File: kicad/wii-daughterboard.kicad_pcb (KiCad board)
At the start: 2 copper layers, 35.2 x 47.6 mm, 34 parts, among them J1 Data, J10 USB, J11 A/V Out, J12 Bluetooth Sync, J14 Case Panel, J2 DC In, J3 GameCube 1, J4 GameCube 2, J5 Bluetooth, J6 GameCube 3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

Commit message: v2.0
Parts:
- removed J14: Case Panel, project-footprints:SFV4R3STBE1HLF
- removed U4: MIC94053YC6-TR, Package_TO_SOT_SMD:SOT-363_SC-70-6_Handsoldering
- added J9: Fr. Panel, project-footprints:SFV4R3STBE1HLF, F.Cu at (77.8, 76.4)
- added Q1: DMG2301L, Package_TO_SOT_SMD:SOT-23_Handsoldering, F.Cu at (74.1, 59.0)
- added R8: 100R, Resistor_SMD:R_0603_1608Metric_Pad1.05x0.95mm_HandSolder, F.Cu at (72.0, 74.4)
- added TP1: 5V, TestPoint:TestPoint_Pad_D1.0mm, F.Cu at (75.5, 56.0)
- added TP2: 3V3, TestPoint:TestPoint_Pad_D1.0mm, F.Cu at (87.4, 55.9)
- added TP3: 1V15, TestPoint:TestPoint_Pad_D1.0mm, F.Cu at (99.3, 55.9)
- added TP4: 1V0, TestPoint:TestPoint_Pad_D1.0mm, F.Cu at (111.2, 55.9)
- C1, C2, C3, C4, C5, C6, L1, L2, L3, U1, U2, U3: moved to F.Cu
- J10: value USB -> A/V Pwr; footprint Connector_JST:JST_SH_BM04B-SRSS-TB_1x04-1MP_P1.00mm_Vertical -> Connector_JST:JST_PH_B2B-PH-SM4-TB_1x02-1MP_P2.00mm_Vertical
- J11: value A/V Out -> Sync; footprint Connector_JST:JST_PH_B2B-PH-SM4-TB_1x02-1MP_P2.00mm_Vertical -> Connector_JST:JST_SH_BM02B-SRSS-TB_1x02-1MP_P1.00mm_Vertical
- J12: value Bluetooth Sync -> Fan
- J3: value GameCube 1 -> WaveBird 1; footprint Connector_JST:JST_SH_BM04B-SRSS-TB_1x04-1MP_P1.00mm_Vertical -> Connector_JST:JST_SH_BM03B-SRSS-TB_1x03-1MP_P1.00mm_Vertical
- J4: value GameCube 2 -> WaveBird 2; footprint Connector_JST:JST_SH_BM04B-SRSS-TB_1x04-1MP_P1.00mm_Vertical -> Connector_JST:JST_SH_BM03B-SRSS-TB_1x03-1MP_P1.00mm_Vertical
- J6: value GameCube 3 -> GC 3/4; footprint Connector_JST:JST_SH_BM04B-SRSS-TB_1x04-1MP_P1.00mm_Vertical -> Connector_JST:JST_SH_BM05B-SRSS-TB_1x05-1MP_P1.00mm_Vertical
- J7: value GameCube 4 -> Mobo Pwr; footprint Connector_JST:JST_SH_BM04B-SRSS-TB_1x04-1MP_P1.00mm_Vertical -> Connector_JST:JST_PH_B4B-PH-SM4-TB_1x04-1MP_P2.00mm_Vertical
- J8: value Motherboard Out -> USB; footprint Connector_JST:JST_PH_B4B-PH-SM4-TB_1x04-1MP_P2.00mm_Vertical -> Connector_JST:JST_SH_BM04B-SRSS-TB_1x04-1MP_P1.00mm_Vertical
- R1: value 66.5K -> 10K; moved to F.Cu
- R2: value 100K -> 66.5K; moved to F.Cu
- R3: value 92K -> 100K; moved to F.Cu
- R4: value 100K -> 92K; moved to F.Cu
- R5: value 453K -> 100K; moved to F.Cu
- R6: value 100K -> 453K; moved to F.Cu
- R7: value 100R -> 100K
- moved C4 79.6 mm to (108.0, 61.2), turned to 270 degrees
- moved R2 77.7 mm to (105.0, 60.1), turned to 180 degrees
- moved L1 74.2 mm to (108.0, 55.8), turned to 270 degrees
- moved J3 72.4 mm to (94.4, 94.2), turned to 141 degrees
- moved U1 71.1 mm to (103.2, 57.0), turned to 270 degrees
- moved C1 69.0 mm to (103.3, 54.4), turned to 0 degrees
- moved J12 68.3 mm to (113.0, 69.4), turned to 270 degrees
- moved J7 64.2 mm to (103.8, 98.8), turned to 141 degrees
- moved J6 63.6 mm to (110.9, 104.9), turned to 231 degrees
- moved R3 62.2 mm to (105.0, 62.4), turned to 0 degrees
- moved J10 60.9 mm to (110.7, 77.4), turned to 270 degrees
- moved J4 56.8 mm to (83.8, 85.7), turned to 141 degrees
- moved J1 54.6 mm to (113.0, 89.8)
- moved H2 54.6 mm to (113.3, 63.0)
- moved H1 54.6 mm to (89.0, 90.2)
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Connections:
- C1 pad 1: +5V -> VBUS
- C2 pad 1: +5V -> VBUS
- C3 pad 1: +5V -> VBUS
- J1 pad MP: GND -> (no net)
- J10 pad 2: /USB_D- -> GND
- J10 pad MP: GND -> (no net)
- J11 pad 1: +5V -> /BT_SYNC
- J11 pad 2: GND -> +3V3
- J12 pad 1: /BT_SYNC -> +5V
- J12 pad 2: +3V3 -> GND
- J3 pad 1: +5V -> +3V3
- J3 pad MP: GND -> (no net)
- J4 pad 1: +5V -> +3V3
- J4 pad MP: GND -> (no net)
- J6 pad 2: /GC_3 -> +3V3
- J6 pad 3: GND -> /GC_3
- J6 pad 4: +3V3 -> /GC_4
- J6 pad MP: GND -> (no net)
- J7 pad 1: +5V -> +3V3
- J7 pad 2: /GC_4 -> +1V15
- J7 pad 3: GND -> +1V0
- J7 pad 4: +3V3 -> GND
- J7 pad MP: GND -> (no net)
- J8 pad 1: +3V3 -> +5V
- J8 pad 2: +1V15 -> /USB_D-
- J8 pad 3: +1V0 -> /USB_D+
- R1 pad 1: +1V0 -> VBUS
- R1 pad 2: Net-(R1-Pad2) -> /ON_OFF
- R2 pad 1: Net-(R1-Pad2) -> +1V0
- R2 pad 2: GND -> Net-(R2-Pad2)
- R3 pad 1: +1V15 -> Net-(R2-Pad2)
- R3 pad 2: Net-(R3-Pad2) -> GND
- R4 pad 1: Net-(R3-Pad2) -> +1V15
- R4 pad 2: GND -> Net-(R4-Pad2)
- R5 pad 1: +3V3 -> Net-(R4-Pad2)
- R5 pad 2: Net-(R5-Pad2) -> GND
- R6 pad 1: Net-(R5-Pad2) -> +3V3
- R6 pad 2: GND -> Net-(R6-Pad2)
- R7 pad 1: Net-(J14-Pad1) -> Net-(R6-Pad2)
- R7 pad 2: +5V -> GND
- U1 pad 3: +5V -> VBUS
- U1 pad 5: Net-(R1-Pad2) -> Net-(R2-Pad2)
- U2 pad 3: +5V -> VBUS
- U2 pad 5: Net-(R3-Pad2) -> Net-(R4-Pad2)
- U3 pad 3: +5V -> VBUS
- U3 pad 5: Net-(R5-Pad2) -> Net-(R6-Pad2)
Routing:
- net +3V3: track 0.00 -> 141.7 mm, vias 0 -> 5
- net +5V: track 0.00 -> 128.3 mm, vias 0 -> 5
- net +1V0: track 0.00 -> 68.4 mm, vias 0 -> 2
- net VBUS: track 0.00 -> 62.7 mm, vias 0 -> 2
- net +1V15: track 0.00 -> 61.0 mm, vias 0 -> 2
- net GND: track 37.5 -> 89.7 mm, vias 0 -> 14
- net /RST: track 0.00 -> 43.7 mm, vias 0 -> 2
- net /GC_2: track 0.00 -> 31.7 mm, vias 0 -> 2
- net /GC_1: track 0.00 -> 20.3 mm, vias 0 -> 2
- net /BT_SYNC: track 0.00 -> 19.4 mm, vias 0 -> 2
- net /GC_4: track 0.00 -> 19.1 mm
- net /ON_OFF: track 0.00 -> 18.6 mm, vias 0 -> 2
- net /GC_3: track 0.00 -> 17.6 mm
- net /USB_D-: track 30.5 -> 44.4 mm
- net /USB_D+: track 30.8 -> 44.4 mm
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- removed copper zone on B.Cu, net +1V0
- removed copper zone on B.Cu, net +1V15
- removed copper zone on B.Cu, net +3V3
- removed copper zone on B.Cu, net +5V
- removed copper zone on B.Cu, net Net-(L1-Pad1)
- removed copper zone on B.Cu, net Net-(L2-Pad1)
- removed copper zone on B.Cu, net Net-(L3-Pad1)
- removed copper zone on B.Cu, net Net-(R1-Pad2)
- removed copper zone on B.Cu, net Net-(R3-Pad2)
- removed copper zone on B.Cu, net Net-(R5-Pad2)
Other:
- board size 35.2 x 47.6 mm -> 44.7 x 59.1 mm
- board text added: "@loopj"
- board text added: "Wii Daughterboard"
- board text added: "v2.0"

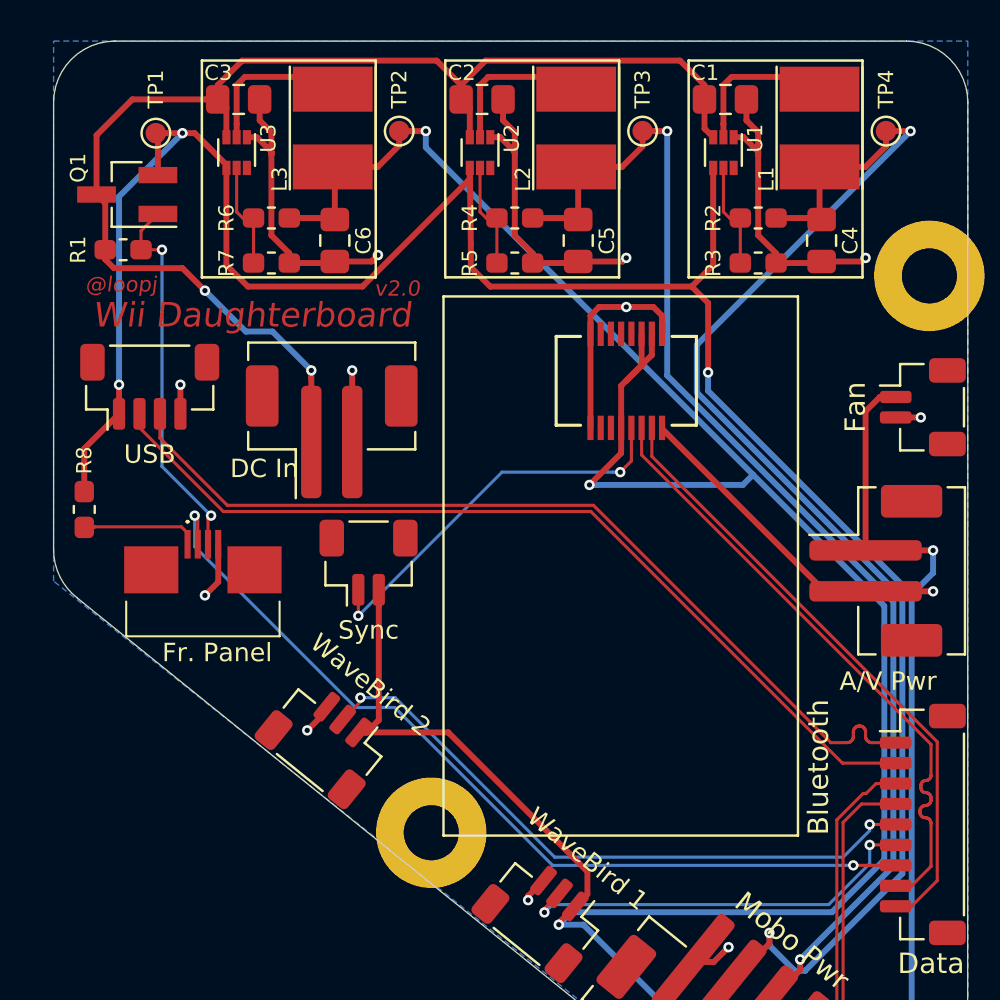
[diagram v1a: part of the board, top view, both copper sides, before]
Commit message: Fix mosfet bug
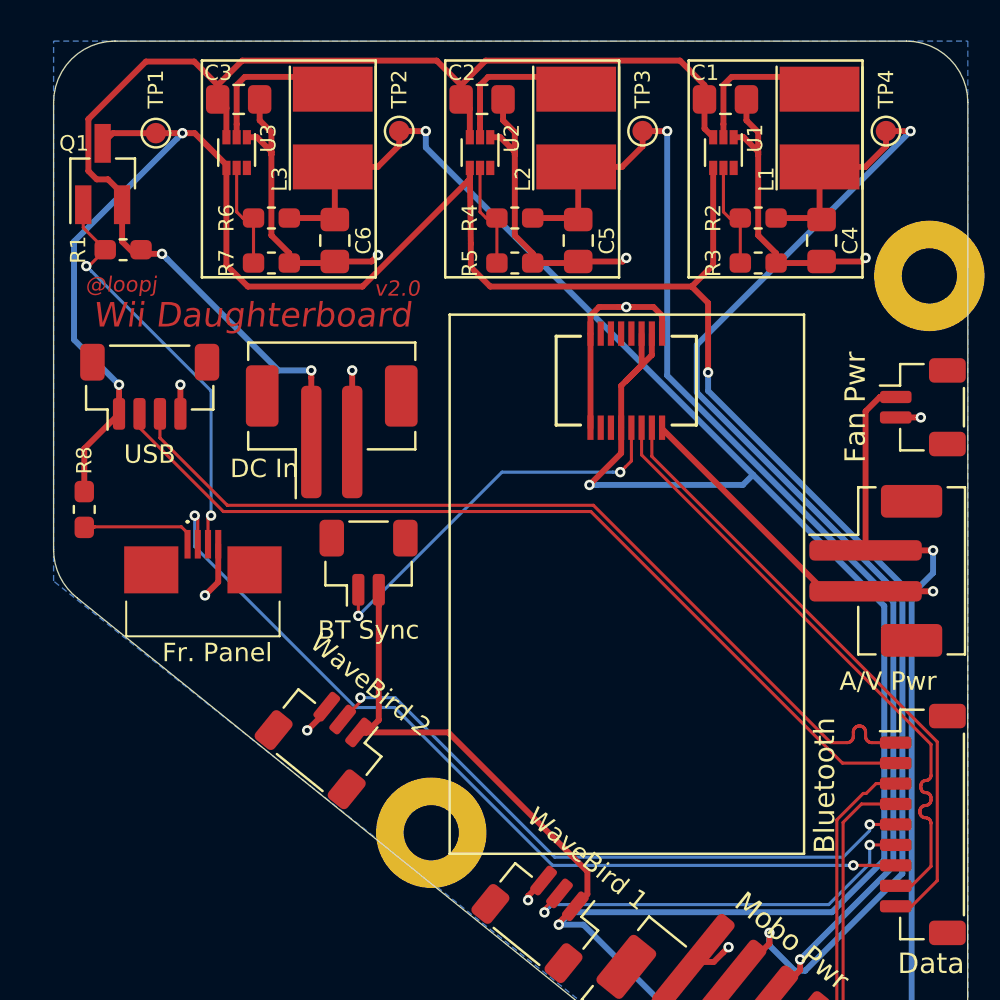
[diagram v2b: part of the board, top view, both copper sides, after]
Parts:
- J11: value Sync -> BT Sync
- J12: value Fan -> Fan Pwr
- R4: value 92K -> 91K
- R8: value 100R -> 150R
- moved Q1 1.56 mm to (72.9, 58.0), turned to 90 degrees
- moved J5 0.89 mm to (98.5, 78.7)
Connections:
- Q1 pad 2: +5V -> VBUS
- Q1 pad 3: VBUS -> +5V
- R1 pad 1: VBUS -> /ON_OFF
- R1 pad 2: /ON_OFF -> VBUS
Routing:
- net +5V: track 128.3 -> 131.0 mm
- net VBUS: track 62.7 -> 64.1 mm
- net /ON_OFF: track 18.6 -> 19.7 mm

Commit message: v3.0
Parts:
- removed J8: USB, Connector_JST:JST_SH_BM04B-SRSS-TB_1x04-1MP_P1.00mm_Vertical
- removed TP1: 5V, TestPoint:TestPoint_Pad_D1.0mm
- removed TP2: 3V3, TestPoint:TestPoint_Pad_D1.0mm
- removed TP3: 1V15, TestPoint:TestPoint_Pad_D1.0mm
- removed TP4: 1V0, TestPoint:TestPoint_Pad_D1.0mm
- added C7: C, Capacitor_SMD:C_0603_1608Metric_Pad1.05x0.95mm_HandSolder, F.Cu at (88.9, 84.1)
- added C8: C, Capacitor_SMD:C_0603_1608Metric_Pad1.05x0.95mm_HandSolder, F.Cu at (98.5, 91.5)
- added C9: C, Capacitor_SMD:C_0603_1608Metric_Pad1.05x0.95mm_HandSolder, F.Cu at (113.5, 75.4)
- added D1: D, Diode_SMD:D_SOD-123, F.Cu at (110.5, 57.9)
- added R9: 1K, Resistor_SMD:R_0603_1608Metric_Pad1.05x0.95mm_HandSolder, F.Cu at (75.3, 72.0)
- C1, C2, C3, C4, C5, C6: footprint Capacitor_SMD:C_0805_2012Metric_Pad1.15x1.40mm_HandSolder -> Capacitor_SMD:C_0603_1608Metric_Pad1.05x0.95mm_HandSolder
- J1: footprint Connector_JST:JST_SH_BM09B-SRSS-TB_1x09-1MP_P1.00mm_Vertical -> Connector_JST:JST_SH_BM07B-SRSS-TB_1x07-1MP_P1.00mm_Vertical
- J10: value A/V Pwr -> A/V; footprint Connector_JST:JST_PH_B2B-PH-SM4-TB_1x02-1MP_P2.00mm_Vertical -> Connector_JST:JST_SH_BM02B-SRSS-TB_1x02-1MP_P1.00mm_Vertical
- J11: value BT Sync -> Sync
- J12: value Fan Pwr -> Fan
- J2: value DC In -> DC
- J3: value WaveBird 1 -> GC 1
- J4: value WaveBird 2 -> GC 2
- J7: footprint Connector_JST:JST_PH_B4B-PH-SM4-TB_1x04-1MP_P2.00mm_Vertical -> Connector_JST:JST_PH_S4B-PH-SM4-TB_1x04-1MP_P2.00mm_Horizontal
- L1, L2, L3: footprint Inductor_SMD:L_Taiyo-Yuden_NR-40xx_HandSoldering -> project-footprints:INDPM3630X200N
- moved R2 31.1 mm to (73.9, 60.0), turned to 90 degrees
- moved R3 29.1 mm to (75.9, 60.0), turned to 270 degrees
- moved C4 29.1 mm to (79.0, 62.4), turned to 180 degrees
- moved L1 25.7 mm to (82.7, 60.4)
- moved U1 24.8 mm to (78.5, 59.0), turned to 180 degrees
- moved C1 24.4 mm to (79.0, 56.4), turned to 180 degrees
- moved C3 23.4 mm to (102.9, 56.4), turned to 180 degrees
- moved U3 23.0 mm to (102.4, 59.0), turned to 180 degrees
- moved L3 22.9 mm to (106.6, 60.4)
- moved R7 18.8 mm to (99.8, 60.0), turned to 270 degrees
- moved C6 18.7 mm to (102.9, 62.4), turned to 180 degrees
- moved R6 16.7 mm to (97.8, 60.0), turned to 90 degrees
- moved J3 13.3 mm to (84.1, 85.8)
- moved J4 13.3 mm to (94.2, 93.9)
- moved R1 11.0 mm to (77.7, 72.0), turned to 270 degrees
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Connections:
- J1 pad 1: /USB_D+ -> /BT_D-
- J1 pad 2: /USB_D- -> /BT_D+
- J1 pad 3: /GC_4 -> /RST
- J1 pad 4: /GC_3 -> /GC_1
- J1 pad 6: /GC_1 -> /GC_3
- J1 pad 7: /RST -> /GC_4
- J10 pad 1: +5V -> Net-(C10-Pad2)
- J12 pad 1: +5V -> +3V3
- J7 pad 1: +3V3 -> GND
- J7 pad 2: +1V15 -> +1V0
- J7 pad 3: +1V0 -> +1V15
- J7 pad 4: GND -> +3V3
- R1 pad 1: /ON_OFF -> VBUS
- R1 pad 2: VBUS -> /ON_OFF
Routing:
- net GND: track 89.7 -> 29.1 mm, vias 14 -> 35
- net +5V: track 131.0 -> 184.8 mm, vias 5 -> 6
- net /USB_D+: track 44.4 -> 0.00 mm
- net /USB_D-: track 44.4 -> 0.00 mm
- net VBUS: track 64.1 -> 32.7 mm, vias 2 -> 0
- net Net-(C10-Pad2): track 0.00 -> 21.4 mm
- net /GC_1: track 20.3 -> 33.1 mm
- net +1V0: track 68.4 -> 57.5 mm
- net +1V15: track 61.0 -> 50.5 mm
- net /ON_OFF: track 19.7 -> 9.65 mm, vias 2 -> 0
- net /GC_2: track 31.7 -> 22.3 mm
- net +3V3: track 141.7 -> 132.7 mm, vias 5 -> 2
- net Net-(L3-Pad1): track 7.66 -> 0.66 mm
- net Net-(L2-Pad1): track 7.66 -> 0.66 mm
- net Net-(L1-Pad1): track 7.66 -> 0.66 mm
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- added copper zone on F.Cu, net +1V0
- added copper zone on F.Cu, net +1V15
- added copper zone on F.Cu, net +3V3
- added copper zone on F.Cu, net GND
- added copper zone on F.Cu, net Net-(L1-Pad1)
- added copper zone on F.Cu, net Net-(L2-Pad1)
- added copper zone on F.Cu, net Net-(L3-Pad1)
- added copper zone on F.Cu, net VBUS
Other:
- board size 44.7 x 59.1 mm -> 44.7 x 56.1 mm
- net class Power: trace_width 0.29 -> 0.676
- board text added: "v3.0"
- board text removed: "v2.0"

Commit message: v3.1
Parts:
- D1: footprint Diode_SMD:D_SOD-123 -> Diode_SMD:D_SOD-323_HandSoldering
- J3: value GC 1 -> GC1
- J4: value GC 2 -> GC2
- U1, U2, U3: footprint Package_TO_SOT_SMD:SOT-563 -> project-footprints:SOTFL50P160X60-6N
- moved D1 16.4 mm to (112.2, 74.2), turned to 180 degrees
- moved C8 10.4 mm to (91.0, 84.3)
- moved R9 3.18 mm to (78.4, 72.7)
- moved R1 3.18 mm to (80.8, 72.7)
- moved R8 3.18 mm to (76.0, 72.7)
- moved Q1 3.04 mm to (78.2, 67.2)
- moved J5 3.00 mm to (101.5, 78.8)
- moved J2 2.90 mm to (87.5, 70.6)
- moved C1 2.44 mm to (81.0, 57.8)
- moved C2 2.44 mm to (92.9, 57.8)
- moved C3 2.44 mm to (104.9, 57.8)
- moved C4 2.44 mm to (81.0, 63.8)
- moved C5 2.44 mm to (92.9, 63.8)
- moved C6 2.44 mm to (104.9, 63.8)
- moved L1 2.44 mm to (84.7, 61.8)
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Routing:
- net GND: track 29.1 -> 85.0 mm, vias 35 -> 38
- net +5V: track 184.8 -> 136.6 mm
- net Net-(C9-Pad2): track 21.4 -> 6.13 mm
- net +3V3: track 132.7 -> 120.6 mm, vias 2 -> 4
- net VBUS: track 32.7 -> 39.7 mm
- net /BT_SYNC: track 17.4 -> 22.3 mm
- net /BT_D-: track 24.5 -> 21.6 mm
- net /BT_D+: track 24.5 -> 21.6 mm
- net Net-(L1-Pad1): track 0.66 -> 3.42 mm
- net Net-(L3-Pad1): track 0.66 -> 3.42 mm
- net Net-(L2-Pad1): track 0.66 -> 3.42 mm
- net +1V15: track 50.5 -> 48.7 mm
- net /LED_PWR: track 5.79 -> 4.12 mm
- net /RST: track 42.5 -> 41.2 mm
- net +1V0: track 57.5 -> 56.4 mm
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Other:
- board size 44.7 x 56.1 mm -> 41.1 x 54.6 mm
- board text added: "v3.1"
- board text removed: "v3.0"

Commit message: Single GND return from mobo
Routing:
- net GND: track 85.0 -> 77.4 mm, vias 38 -> 34
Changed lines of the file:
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@@
     (thickness 1.6)
     (drawings 26)
-    (tracks 360)
+    (tracks 354)
     (zones 0)
     (modules 39)
@@
   (via (at 112.9 69.4) (size 0.508) (drill 0.254) (layers Top Bottom) (net 1))
   (segment (start 111.675 69.4) (end 112.9 69.4) (width 0.5) (layer Top) (net 1))
-  (via (at 100.3 98.4) (size 0.508) (drill 0.254) (layers Top Bottom) (net 1))
-  (via (at 101 98.9) (size 0.508) (drill 0.254) (layers Top Bottom) (net 1))
-  (via (at 100.9 97.6) (size 0.508) (drill 0.254) (layers Top Bottom) (net 1))
-  (via (at 101.6 98.1) (size 0.508) (drill 0.254) (layers Top Bottom) (net 1))
-  (segment (start 100.9 96.759298) (end 103.162125 94.497173) (width 0.68) (layer Top) (net 1))
-  (segment (start 100.9 97.6) (end 100.9 96.759298) (width 0.68) (layer Top) (net 1))
   (via (at 88.1 66.8) (size 0.508) (drill 0.254) (layers Top Bottom) (net 1))
   (via (at 88.8 66.8) (size 0.508) (drill 0.254) (layers Top Bottom) (net 1))
@@
   (via (at 88.8 67.5) (size 0.508) (drill 0.254) (layers Top Bottom) (net 1))
   (segment (start 88.5 71.1) (end 88.5 67.2) (width 0.68) (layer Top) (net 1))
-  (segment (start 105.2 81.7) (end 105.2 92.459298) (width 0.68) (layer Top) (net 1) (status 1000000))
-  (segment (start 105.2 92.459298) (end 103.162125 94.497173) (width 0.68) (layer Top) (net 1) (status 1000000))
-  (segment (start 95.1 71.6) (end 105.2 81.7) (width 0.68) (layer Top) (net 1) (status 1000000))
-  (segment (start 89 71.6) (end 95.1 71.6) (width 0.68) (layer Top) (net 1) (status 1000000))
-  (segment (start 88.5 71.1) (end 89 71.6) (width 0.68) (layer Top) (net 1) (status 1000000))
+  (segment (start 103.6 83.8) (end 103.6 94.059298) (width 1) (layer Top) (net 1))
+  (segment (start 103.6 94.059298) (end 103.162125 94.497173) (width 1) (layer Top) (net 1))
+  (segment (start 91.4 71.6) (end 103.6 83.8) (width 1) (layer Top) (net 1))
+  (segment (start 89 71.6) (end 91.4 71.6) (width 1) (layer Top) (net 1))
+  (segment (start 88.5 71.1) (end 89 71.6) (width 1) (layer Top) (net 1))
   (via (at 95.775 68.025) (size 0.508) (drill 0.254) (layers Top Bottom) (net 5))
   (via (at 112.95 89.8) (size 0.508) (drill 0.254) (layers Top Bottom) (net 9))
@@
       )
     )
-  )
-  (zone (net 1) (net_name GND) (layer Top) (hatch edge 0.508)
-    (connect_pads yes (clearance 0.1))
-    (min_thickness 0.254)
-    (fill yes (arc_segments 32) (thermal_gap 0.508) (thermal_bridge_width 0.508))
-    (polygon
-      (pts
-        (xy 102.8 97.9) (xy 101 100.1) (xy 99 98.5) (xy 100.8 96.3)
-      )
-    )

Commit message: Nicer diode label
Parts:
- moved D1 0.30 mm to (111.9, 74.2)
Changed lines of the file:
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@@
     (thickness 1.6)
     (drawings 26)
-    (tracks 354)
+    (tracks 353)
     (zones 0)
     (modules 39)
@@
   )
   (setup
-    (last_trace_width 0.68)
+    (last_trace_width 0.5)
     (user_trace_width 0.17)
     (user_trace_width 0.3)
@@
   )
   (module Diode_SMD:D_SOD-323_HandSoldering (layer Top)
-    (at 112.2 74.25 180)
+    (at 111.9 74.25 180)
     (descr SOD-323)
     (tags SOD-323)
     (attr smd)
-    (fp_text reference D1 (at 0 -0.05) (layer F.SilkS)
+    (fp_text reference D1 (at -2.6 0.15 270) (layer F.SilkS)
       (effects (font (size 0.75 0.75) (thickness 0.1)))
     )
@@
     (tags "capacitor handsolder")
     (attr smd)
-    (fp_text reference C9 (at 2.2 0) (layer F.SilkS)
+    (fp_text reference C9 (at 2.3 0 90) (layer F.SilkS)
       (effects (font (size 0.75 0.75) (thickness 0.1)))
     )
@@
       (effects (font (size 1 1) (thickness 0.15)))
     )
-    (fp_text value Fan (at 3.5 -0.7 180) (layer F.SilkS)
+    (fp_text value Fan (at 3.2 -0.7 180) (layer F.SilkS)
       (effects (font (size 0.9 0.9) (thickness 0.15)))
     )
@@
       (effects (font (size 1 1) (thickness 0.15)))
     )
-    (fp_text value A/V (at 3.3 -0.6 180) (layer F.SilkS)
+    (fp_text value A/V (at 3.2 -0.6 180) (layer F.SilkS)
       (effects (font (size 0.9 0.9) (thickness 0.15)))
     )
@@
       (effects (font (size 1 1) (thickness 0.15)))
     )
-    (fp_text value Data (at 5.8 -0.4 180) (layer F.SilkS)
+    (fp_text value Data (at 5.7 -0.4 180) (layer F.SilkS)
       (effects (font (size 0.9 0.9) (thickness 0.15)))
     )
@@
   (segment (start 91 59.9) (end 90.8 59.7) (width 0.3) (layer Top) (net 2))
   (segment (start 91.562 59.9) (end 91 59.9) (width 0.3) (layer Top) (net 2))
-  (segment (start 110.9 74.45) (end 110.95 74.5) (width 0.5) (layer Top) (net 2))
-  (segment (start 110.9 74.2) (end 110.95 74.25) (width 0.5) (layer Top) (net 2))
-  (segment (start 110.9 73) (end 110.9 74.2) (width 0.5) (layer Top) (net 2))
   (via (at 106.55 77.350004) (size 0.508) (drill 0.254) (layers Top Bottom) (net 2))
   (segment (start 110.9 73) (end 106.55 77.35) (width 0.3) (layer Bottom) (net 2))
@@
   (segment (start 103.7 65.8) (end 110.646001 72.746001) (width 0.5) (layer Bottom) (net 2))
   (segment (start 77.299996 65.8) (end 103.7 65.8) (width 0.5) (layer Bottom) (net 2))
+  (segment (start 110.9 74) (end 110.65 74.25) (width 0.5) (layer Top) (net 2))
+  (segment (start 110.9 73) (end 110.9 74) (width 0.5) (layer Top) (net 2))
   (segment (start 104.716417 95.755814) (end 104.816417 95.655814) (width 0.68) (layer Top) (net 3))
   (via (at 83.7 63.2) (size 0.508) (drill 0.254) (layers Top Bottom) (net 3))
@@
   (segment (start 99.875 60.4) (end 99.8 60.475) (width 0.3) (layer Top) (net 22))
   (segment (start 103.562 60.4) (end 99.875 60.4) (width 0.3) (layer Top) (net 22))
-  (segment (start 113.45 75.925) (end 113.075 76.3) (width 0.5) (layer Top) (net 23))
-  (segment (start 113.45 74.25) (end 113.45 75.925) (width 0.5) (layer Top) (net 23))
   (segment (start 111.575 77.8) (end 111.575 79.6) (width 0.5) (layer Top) (net 23))
   (segment (start 113.075 76.3) (end 111.575 77.8) (width 0.5) (layer Top) (net 23))
+  (segment (start 113.075 74.325) (end 113.15 74.25) (width 0.5) (layer Top) (net 23))
+  (segment (start 113.075 76.3) (end 113.075 74.325) (width 0.5) (layer Top) (net 23))
   (zone (net 1) (net_name GND) (layer Bottom) (hatch edge 0.508)
     (priority 3)

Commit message: v3.2
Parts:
- H1, H2: footprint MountingHole:MountingHole_2.7mm_Pad -> MountingHole:MountingHole_2.7mm_M2.5_ISO14580_Pad
- moved J5 0.40 mm to (101.5, 79.2)
- moved C7 0.30 mm to (89.0, 84.0)
- moved C8 0.30 mm to (91.0, 84.0)
- moved J4 0.28 mm to (94.3, 94.2)
- moved J9 0.20 mm to (78.9, 76.9)
- moved J10 0.10 mm to (113.0, 80.1)
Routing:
- net +3V3: track 120.6 -> 129.1 mm
- net /BT_D+: track 21.6 -> 27.9 mm
- net +5V: track 136.6 -> 141.6 mm
- net /BT_D-: track 21.6 -> 26.1 mm
- net /BT_SYNC: track 22.3 -> 25.6 mm
- net GND: track 77.4 -> 76.3 mm, vias 34 -> 35
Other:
- board text added: "+"
- board text added: "-"
- board text added: "1V0"
- board text added: "1V15"
- board text added: "3V3"
- board text added: "v3.2"
- board text removed: "v3.1"
